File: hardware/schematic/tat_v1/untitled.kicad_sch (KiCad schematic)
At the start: 29 parts, among them J1 JST-PH 2 Pin, J2 USB_C_Receptacle_USB2.0_14P, SW1 SW_SPDT, U1 BQ25185, U2 USBLC6-2P6, U3 TPS631000DRLR

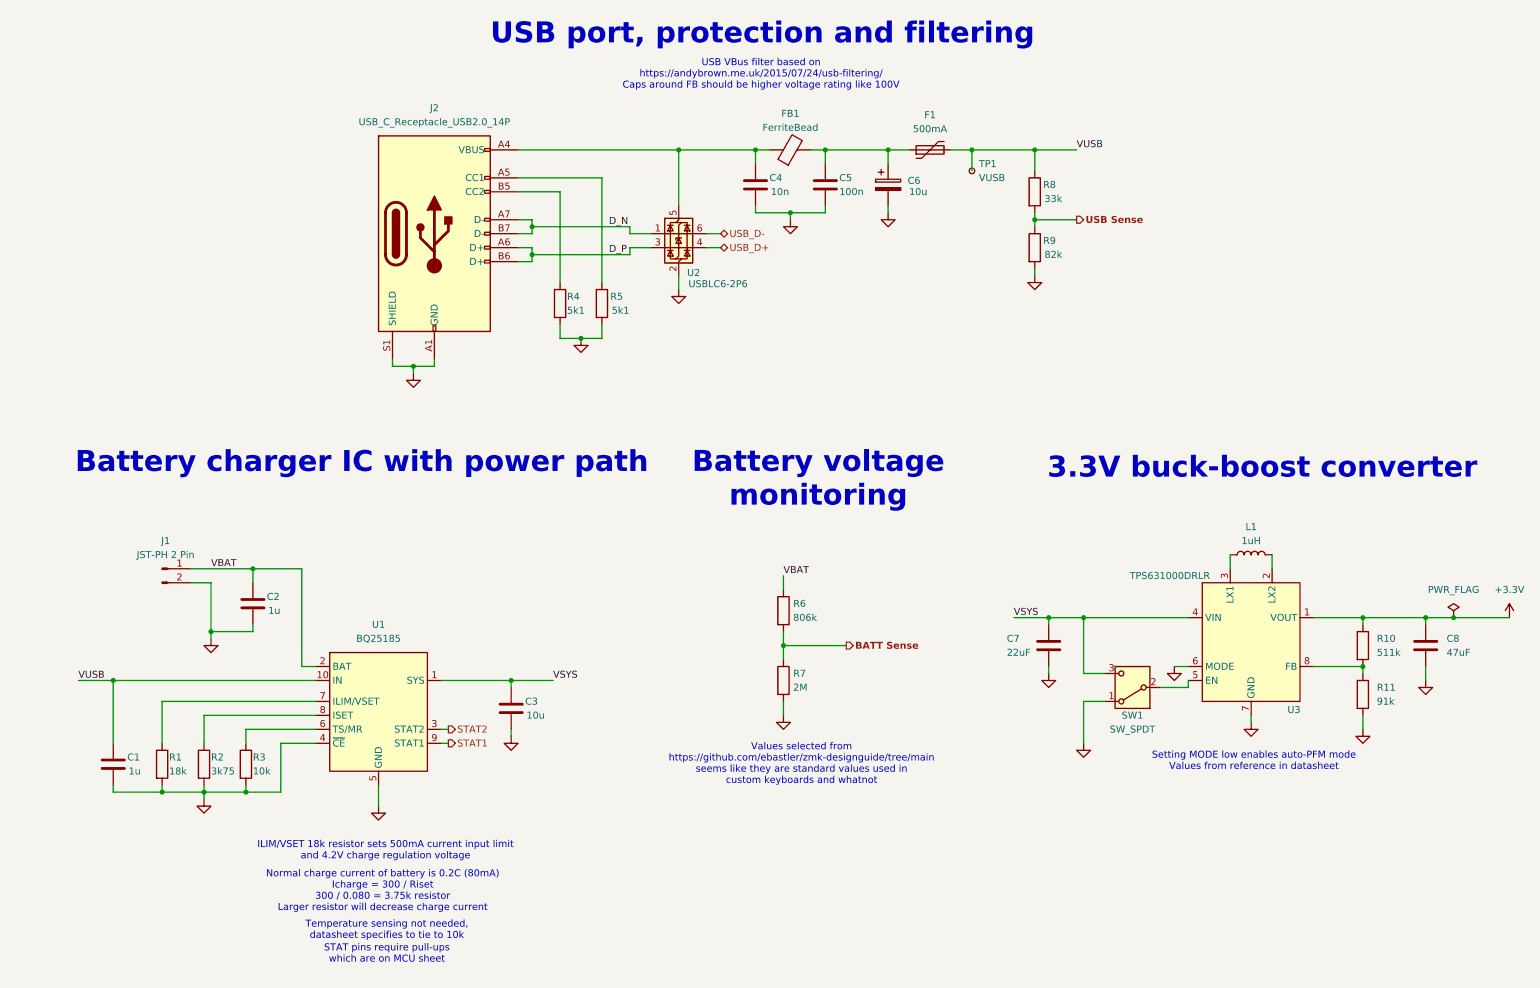
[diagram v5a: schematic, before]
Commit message: Fixed all ERC errors and warnings
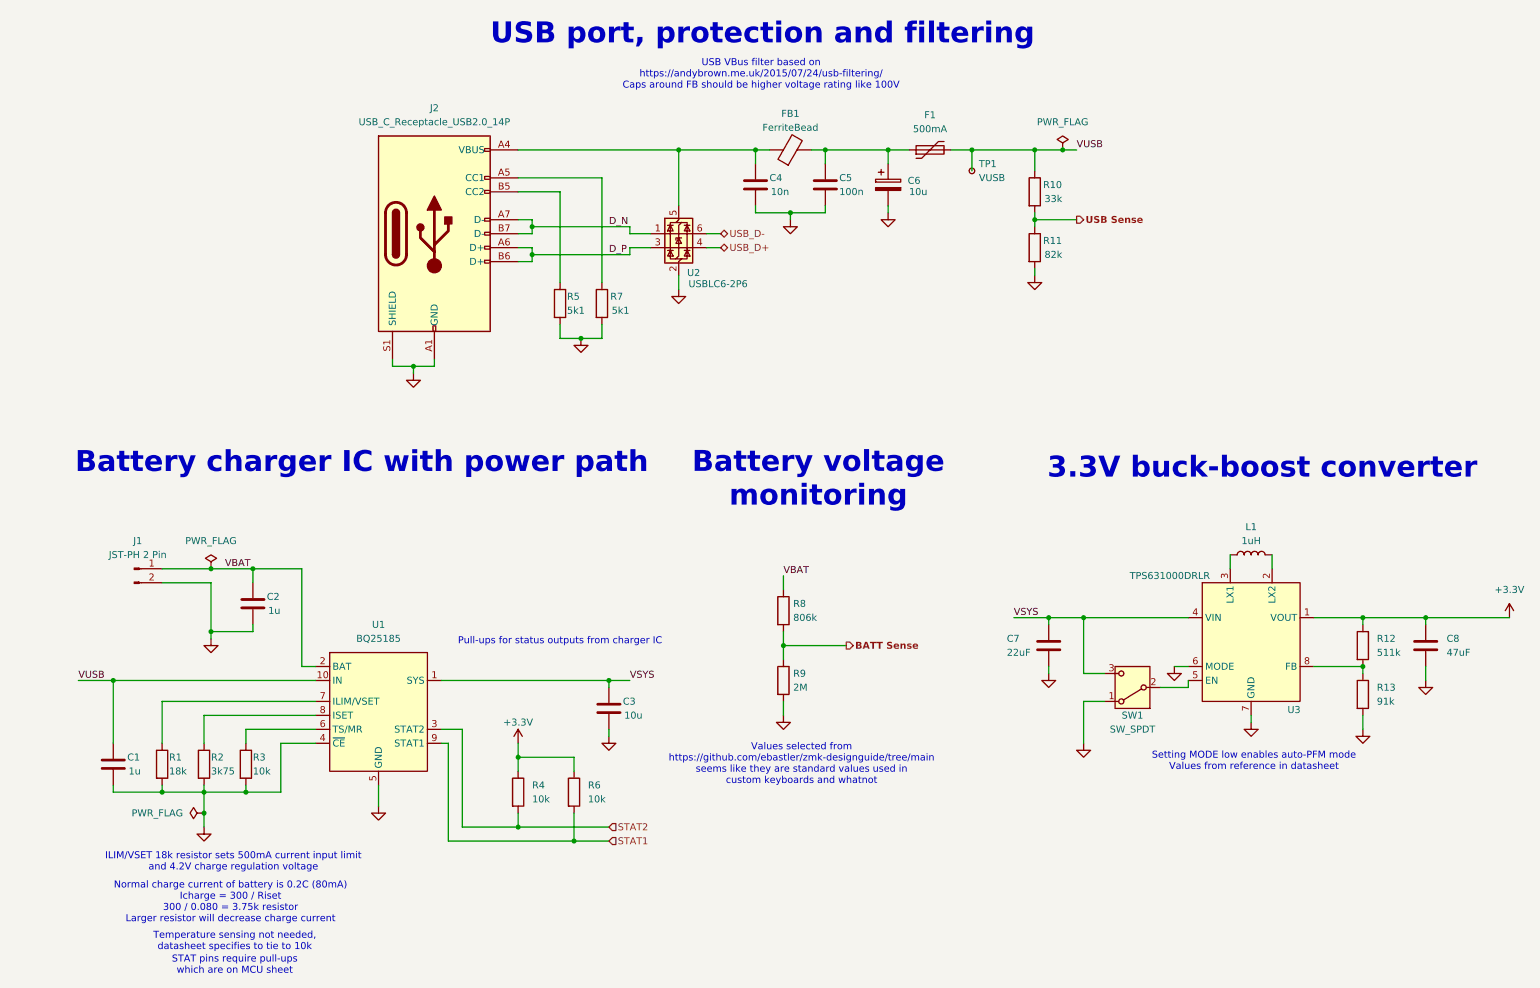
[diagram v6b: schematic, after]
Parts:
- added R4, R6: 10k, symbol Device:R
- renumbered R8 to R10, R9 to R11, R10 to R12, R11 to R13, R4 to R5, R5 to R7, R6 to R8, R7 to R9
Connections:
- net +3.3V: now also R4.1, R6.1
- net STAT1: now also R6.2
- net STAT2: now also R4.2
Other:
- note added: "Pull-ups for status outputs from charger IC"
- moved on the sheet: C3, J1

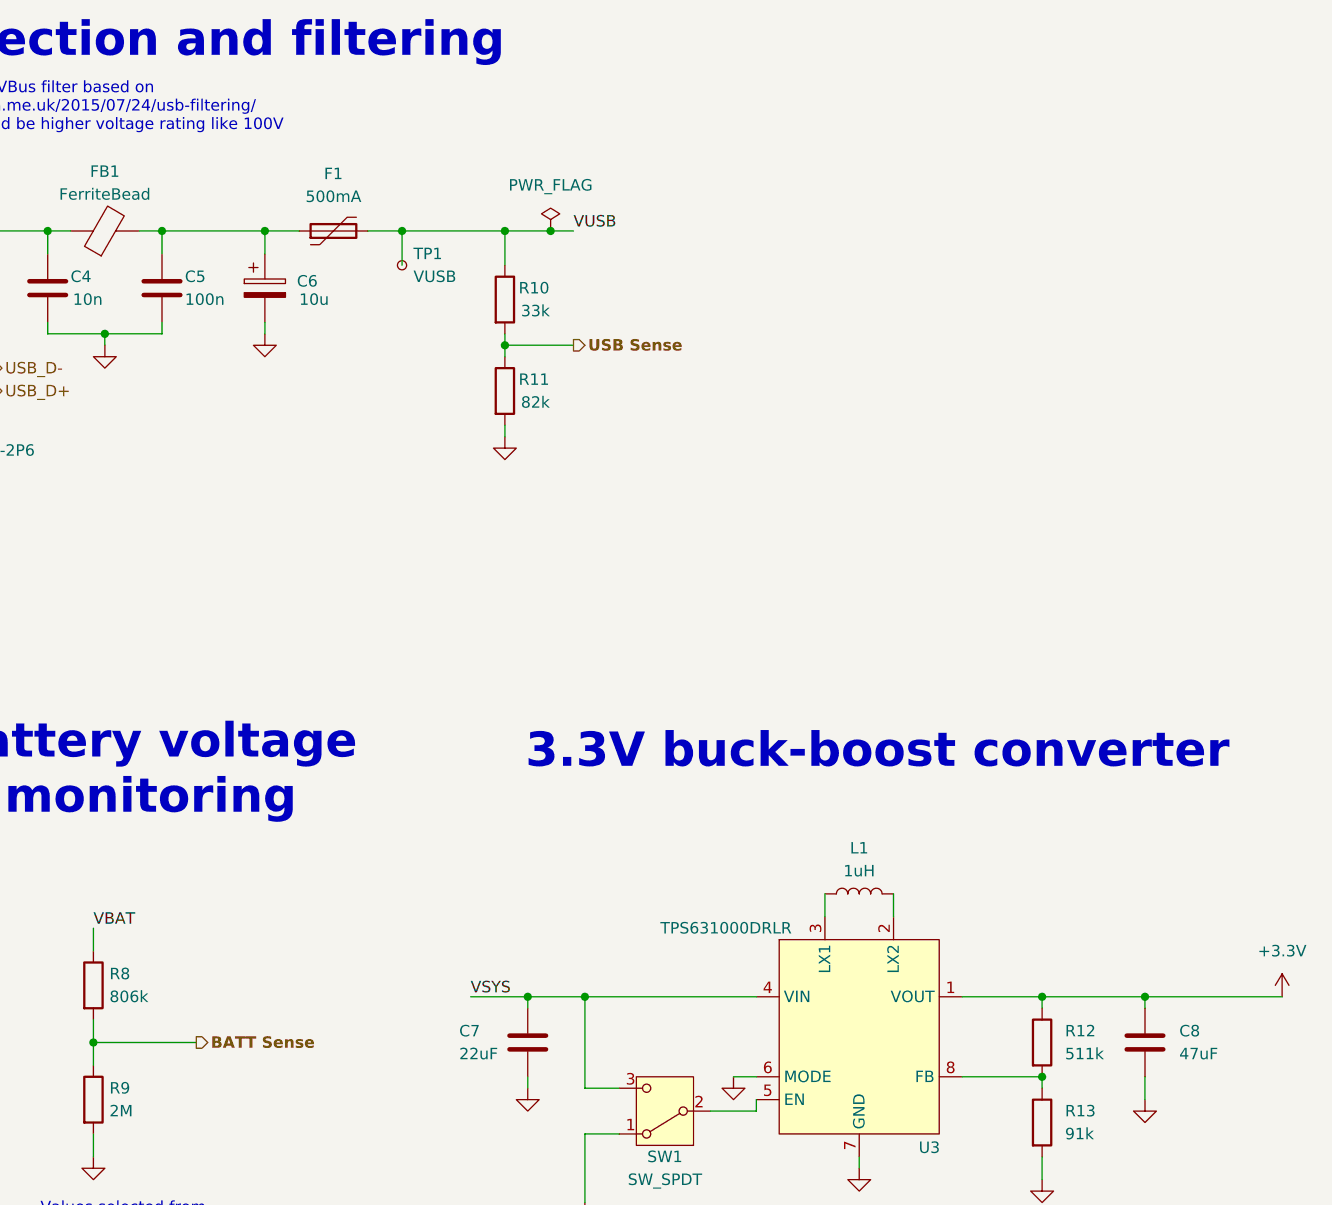
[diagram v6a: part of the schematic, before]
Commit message: Continuing with setting basic footprints for parts
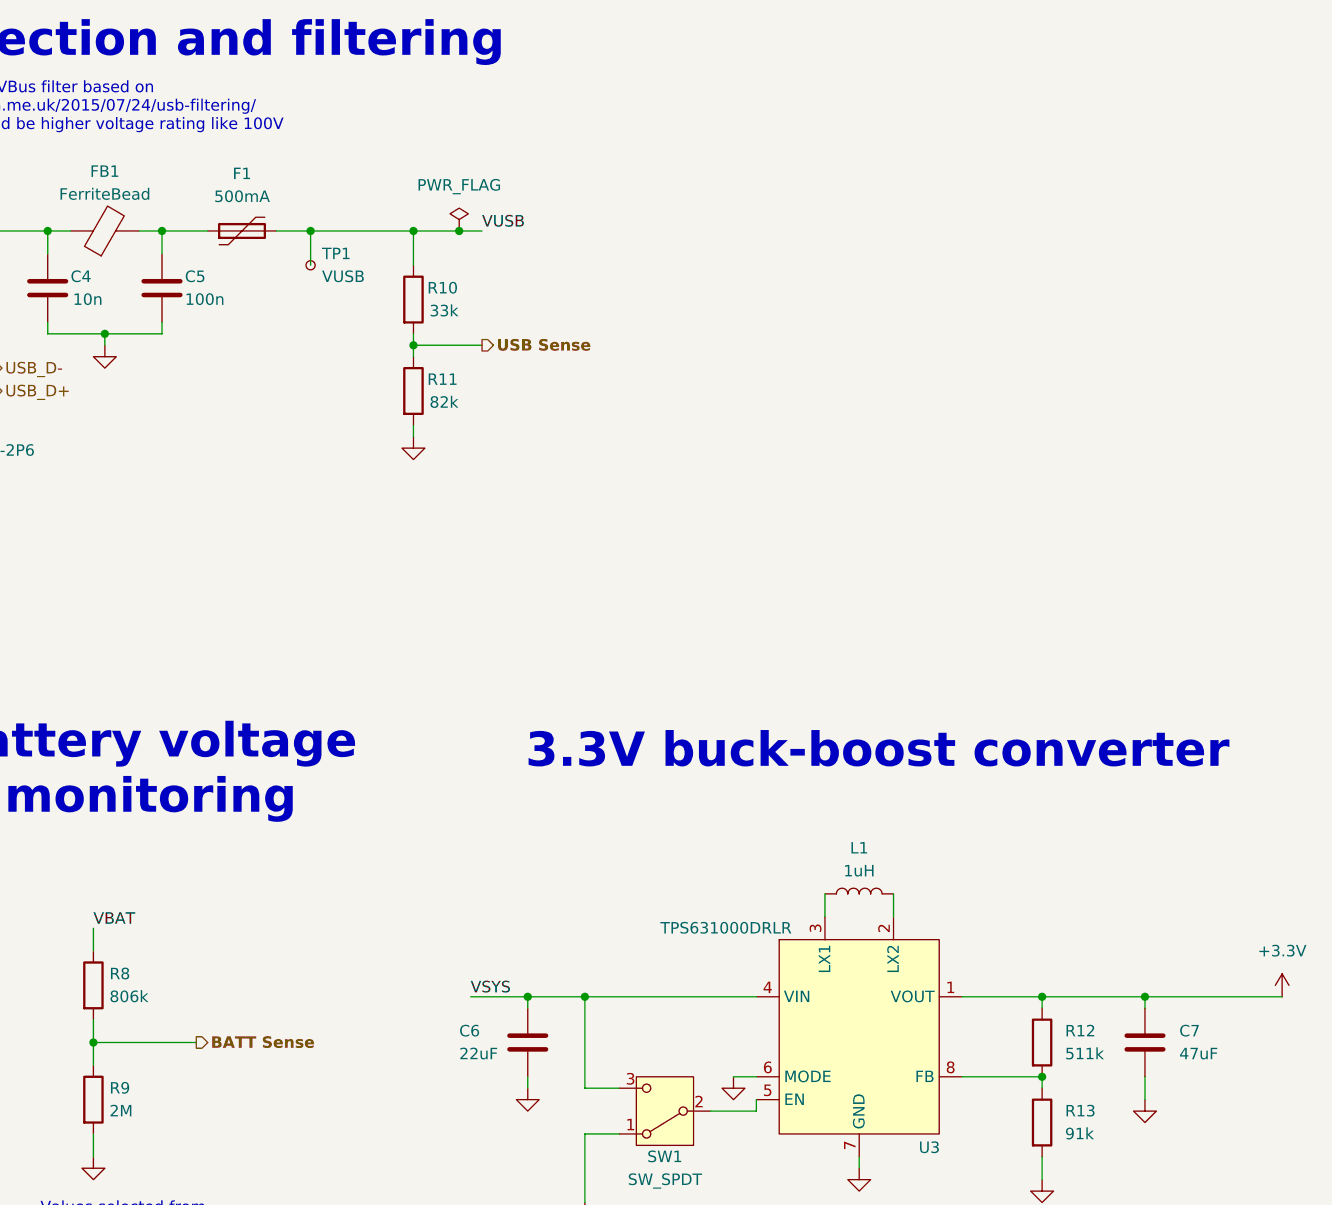
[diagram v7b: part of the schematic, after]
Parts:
- removed C6: 10u, symbol Device:C_Polarized
- C6: renamed from C7; LCSC Link (none) -> https://www.lcsc.com/product-detail/Multilayer-Ceramic-Capa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
- C7: renamed from C8; footprint (none) -> Capacitor_SMD:C_0603_1608Metric; LCSC Link (none) -> https://www.lcsc.com/product-detail/Multilayer-Ceramic-Capa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
- FB1: footprint (none) -> Inductor_SMD:L_0603_1608Metric; LCSC Link (none) -> https://www.lcsc.com/product-detail/Ferrite-Beads_Murata-El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
- L1: footprint (none) -> Inductor_SMD:L_0603_1608Metric; LCSC Link (none) -> https://www.lcsc.com/product-detail/Inductors-SMD_Murata-El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
- R1, R10, R11, R12, R13, R2, R3, R4, R5, R6, R7, R8, R9: footprint (none) -> Resistor_SMD:R_0402_1005Metric
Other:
- moved on the sheet: F1, R10, R11, TP1

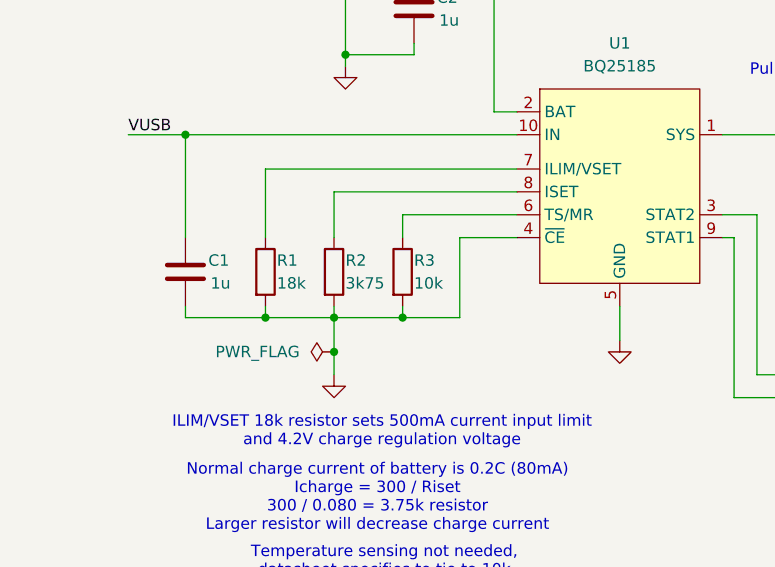
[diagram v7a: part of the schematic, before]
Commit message: Continuing work on setting parts footprints
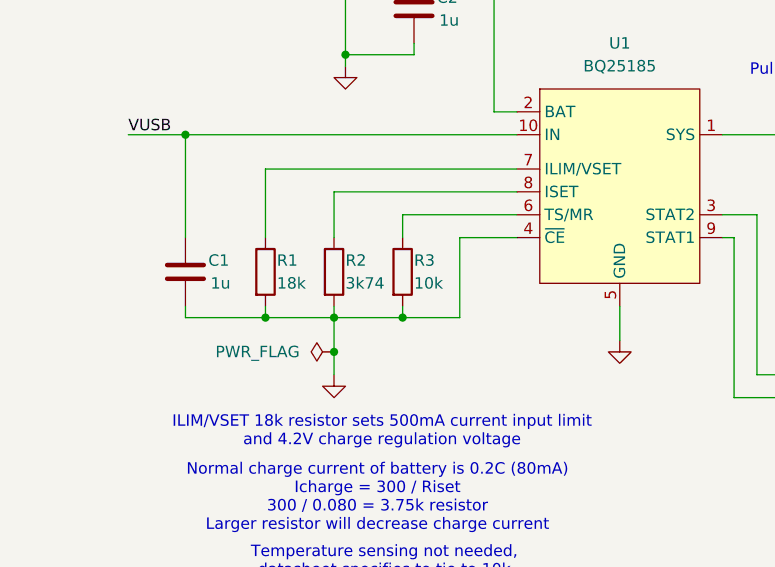
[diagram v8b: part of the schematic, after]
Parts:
- C1, C2: footprint Capacitor_SMD:C_0402_1005Metric -> Capacitor_SMD:C_0603_1608Metric; Link (none) -> https://www.lcsc.com/product-detail/Multilayer-Ceramic-Capa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
- C3: footprint Capacitor_SMD:C_0402_1005Metric -> Capacitor_SMD:C_0805_2012Metric; Link (none) -> https://www.lcsc.com/product-detail/Multilayer-Ceramic-Capa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
- C4, C5: footprint Capacitor_SMD:C_0402_1005Metric -> Capacitor_SMD:C_1206_3216Metric; Link (none) -> https://www.lcsc.com/product-detail/Multilayer-Ceramic-Capa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
- C6, C7: LCSC Link https://www.lcsc.com/product-detail/Multilayer-Ceramic-Capa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 -> (none); Link (none) -> https://www.lcsc.com/product-detail/Multilayer-Ceramic-Capa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
- F1: Link (none) -> https://www.lcsc.com/product-detail/Resettable-Fuses_Littel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
- J2: footprint (none) -> Connector_USB:USB_C_Receptacle_HRO_TYPE-C-31-M-12; Link (none) -> https://www.lcsc.com/product-detail/USB-Connectors_Korean-H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
- L1: LCSC Link https://www.lcsc.com/product-detail/Inductors-SMD_Murata-El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 -> (none); Link (none) -> https://www.lcsc.com/product-detail/Inductors-SMD_Murata-El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
- R1, R10, R11, R12, R13, R3, R4, R5, R6, R7, R8, R9: Link (none) -> https://www.lcsc.com/product-detail/Chip-Resistor-Surface-M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
- R2: value 3k75 -> 3k74; Link (none) -> https://www.lcsc.com/product-detail/Chip-Resistor-Surface-M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
- TP1: footprint (none) -> TestPoint:TestPoint_Pad_D2.0mm
- U2: Link (none) -> https://www.lcsc.com/product-detail/ESD-and-Surge-Protectio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
- U3: footprint (none) -> Package_TO_SOT_SMD:SOT-583-8; Link (none) -> https://www.lcsc.com/product-detail/DC-DC-Converters_Texas-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
